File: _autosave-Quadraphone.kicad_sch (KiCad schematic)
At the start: 29 parts, among them J1 Conn_01x10_Male, J2 Conn_01x10_Male, J3 Conn_01x10_Male, J4 Conn_01x10_Male, J5 Eurorack_10_pin_power, U1 AMS1117-5.0, U14 LM4040DBZ-2.5, U3 MCP6002, U4 LM4040DBZ-5, U5 MCP6004, U8 4066

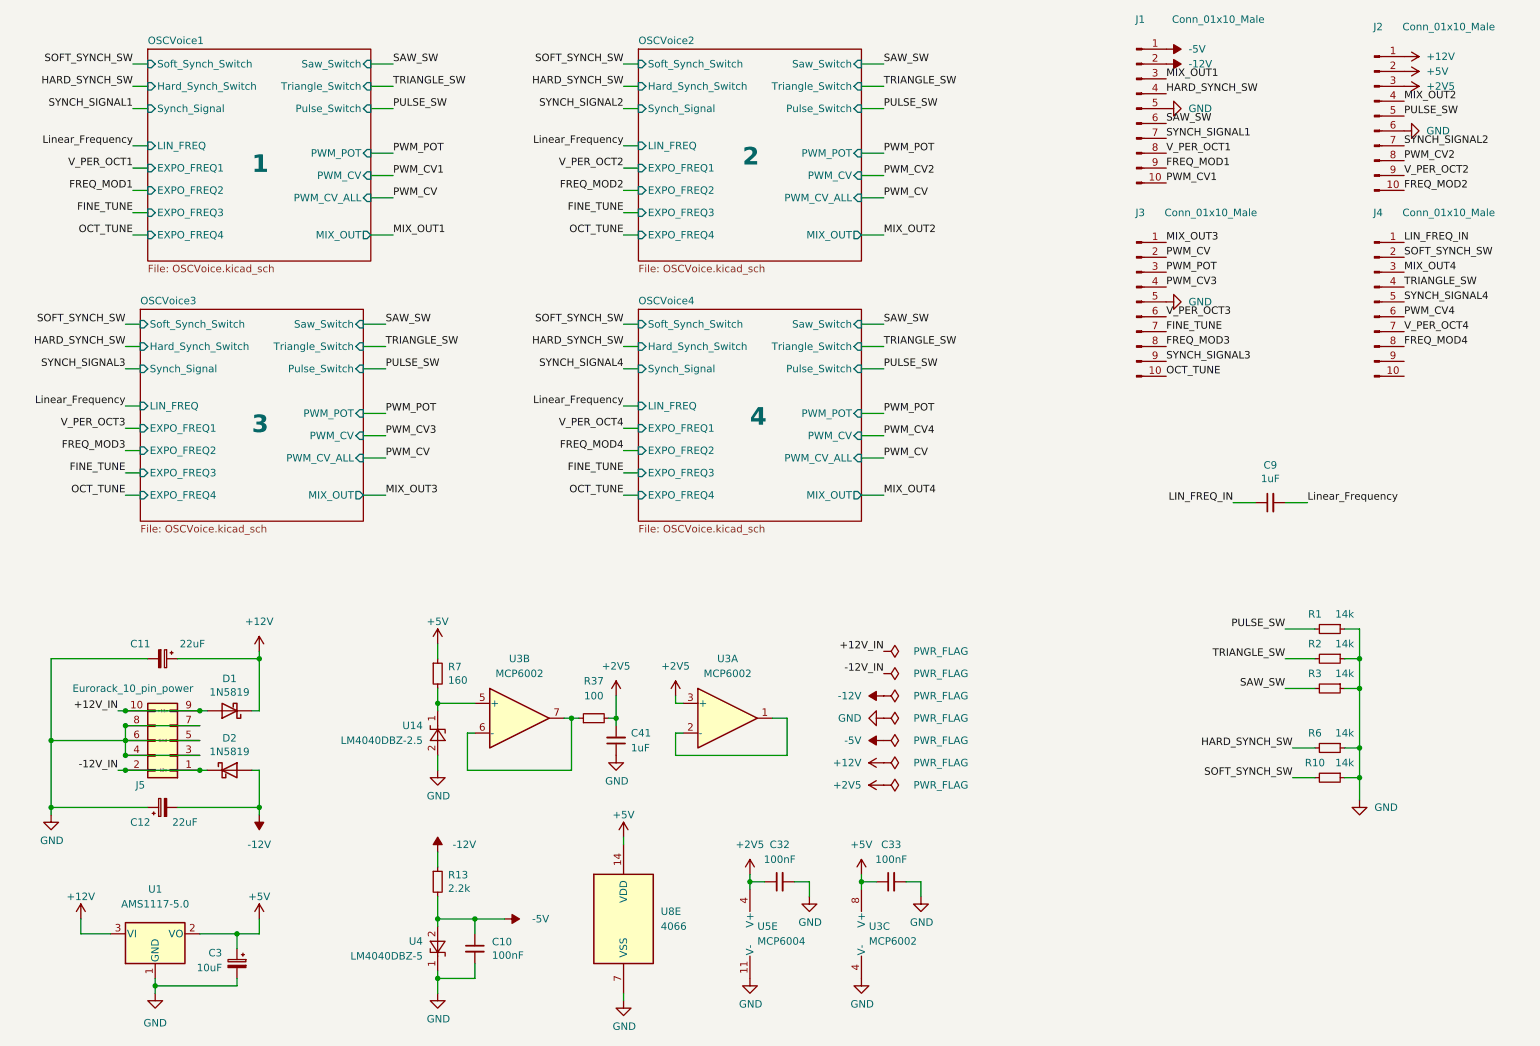
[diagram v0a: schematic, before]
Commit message: Started control board schematic
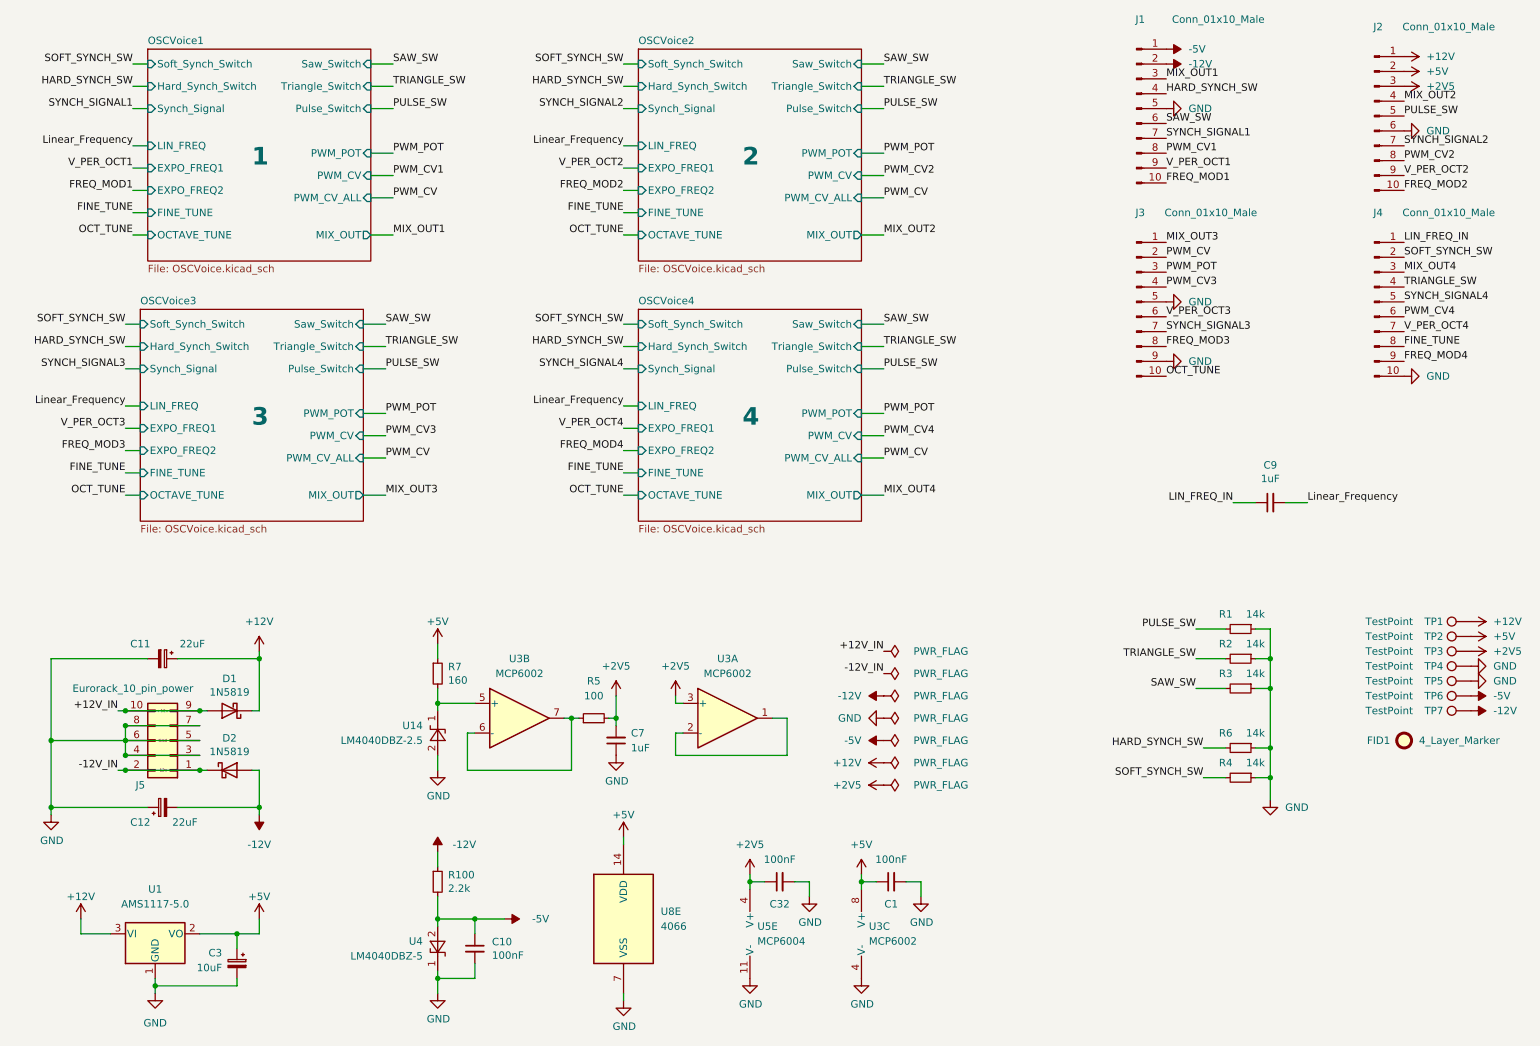
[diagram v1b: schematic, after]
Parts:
- added FID1: 4_Layer_Marker, Custom_Footprints:4_Layer_Markers, symbol Mechanical:Fiducial
- added TP1, TP2, TP3, TP4, TP5, TP6, TP7: TestPoint, Custom_Footprints:1.3mm_Test_Point, symbol Connector:TestPoint
- renumbered C33 to C1, C41 to C7, R13 to R100, R10 to R4, R37 to R5
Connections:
- net +12V: now also TP1.1
- net +2V5: now also TP3.1
- net +5V: now also TP2.1
- net -12V: now also TP7.1
- net -5V: now also TP6.1
- net FINE_TUNE: now also J4.8 (Pin_8); no longer J3.7 (Pin_7)
- net FREQ_MOD1: now also J1.10 (Pin_10); no longer J1.9 (Pin_9)
- net FREQ_MOD4: now also J4.9 (Pin_9); no longer J4.8 (Pin_8)
- net GND: now also J3.9 (Pin_9), J4.10 (Pin_10), TP4.1, TP5.1
- net PWM_CV1: now also J1.8 (Pin_8); no longer J1.10 (Pin_10)
- net SYNCH_SIGNAL3: now also J3.7 (Pin_7); no longer J3.9 (Pin_9)
- net V_PER_OCT1: now also J1.9 (Pin_9); no longer J1.8 (Pin_8)
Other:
- sheet OSCVoice1 ports: added FINE_TUNE, OCTAVE_TUNE; removed EXPO_FREQ3, EXPO_FREQ4
- sheet OSCVoice2 ports: added FINE_TUNE, OCTAVE_TUNE; removed EXPO_FREQ3, EXPO_FREQ4
- sheet OSCVoice3 ports: added FINE_TUNE, OCTAVE_TUNE; removed EXPO_FREQ3, EXPO_FREQ4
- sheet OSCVoice4 ports: added FINE_TUNE, OCTAVE_TUNE; removed EXPO_FREQ3, EXPO_FREQ4
- moved on the sheet: R1, R2, R3, R4, R6
